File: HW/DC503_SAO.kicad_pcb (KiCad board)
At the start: 2 copper layers, 63.1 x 45.1 mm, 34 parts, among them J1 GS2, J2 GS2, U1 ATTINY85-20SU, X1 Badgelife_shitty_connector

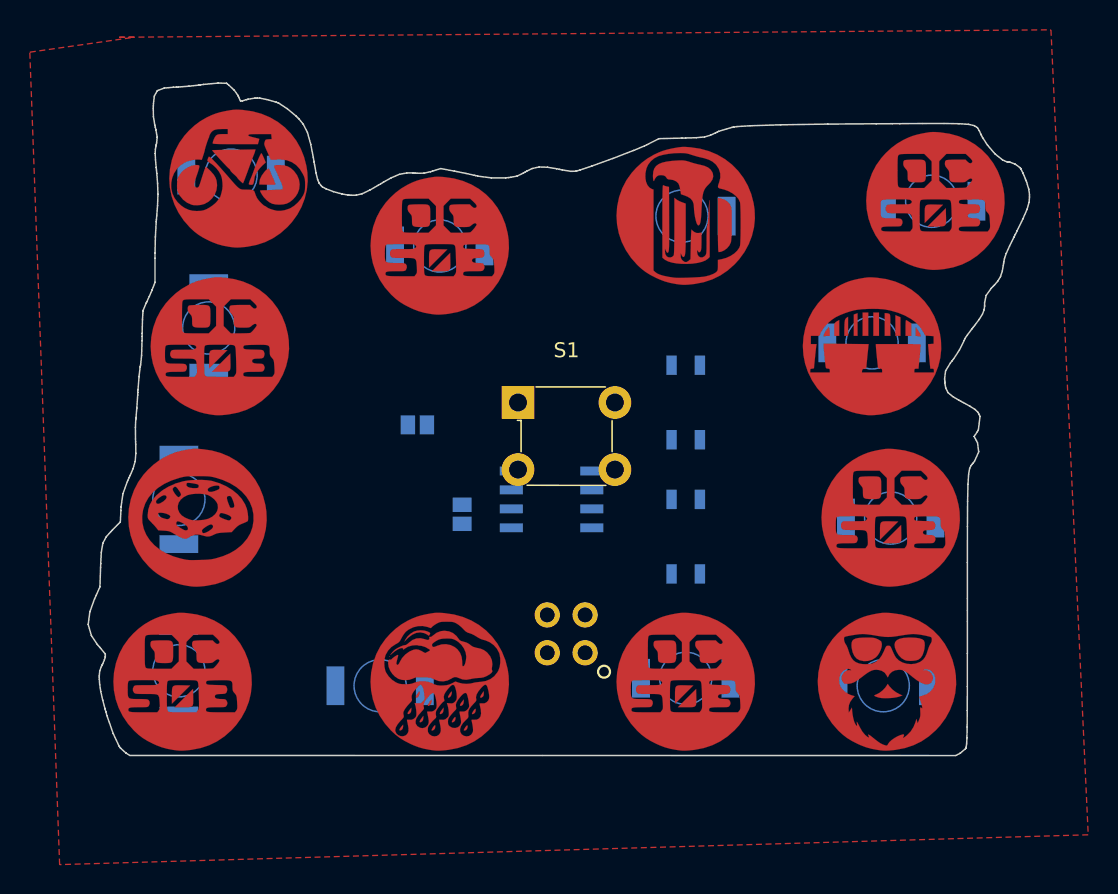
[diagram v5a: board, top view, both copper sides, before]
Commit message: Removed Silk screen from SAO CX placed LEDs move LED ref silk
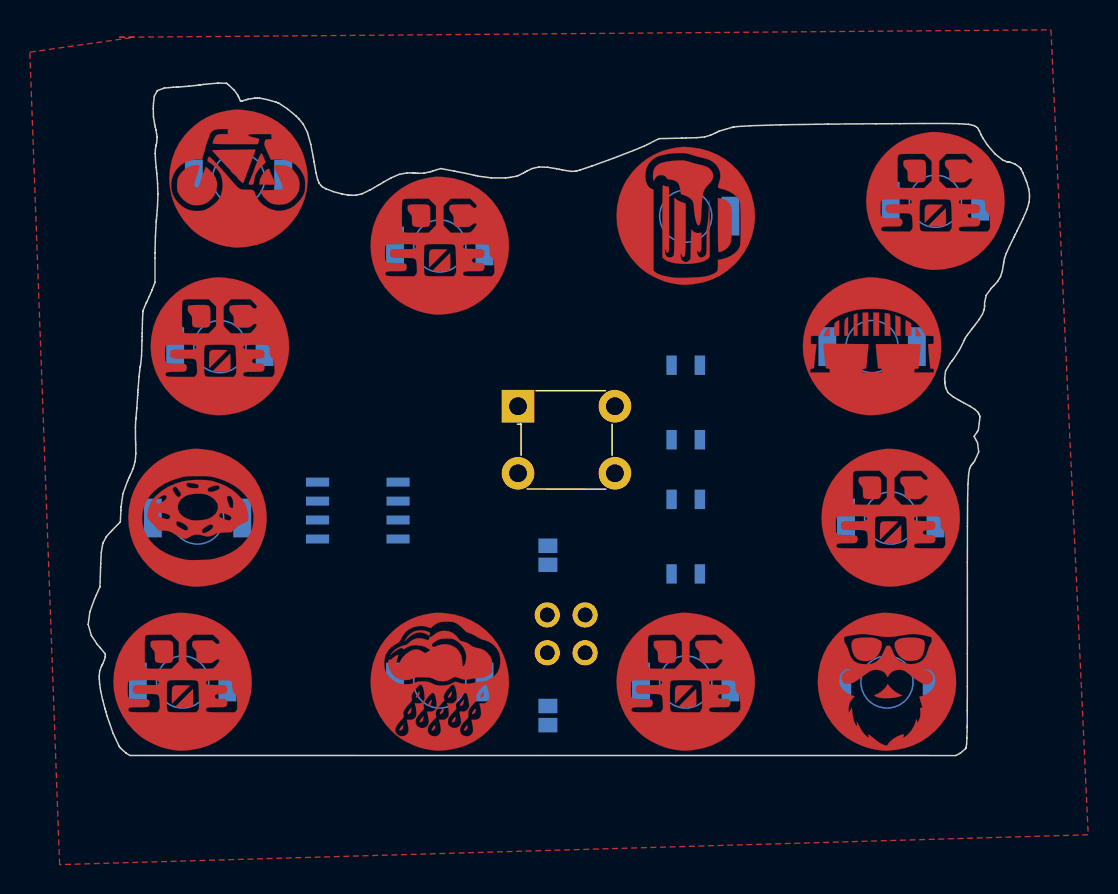
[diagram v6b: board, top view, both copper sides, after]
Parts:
- D1: footprint DC503_SAO:OSRAM_LED -> OSRAM_LED
- moved J2 14.7 mm to (173.8, 106.5)
- moved U1 13.0 mm to (161.0, 92.8)
- moved J1 12.4 mm to (173.8, 95.8), turned to 180 degrees
- moved D9 4.01 mm to (166.5, 104.2), turned to 180 degrees
- moved D11 1.77 mm to (150.2, 93.2), turned to 180 degrees
- moved D12 1.46 mm to (151.8, 81.8), turned to 180 degrees
- moved D10 0.79 mm to (149.2, 104.2), turned to 180 degrees
- moved D1 0.56 mm to (153.0, 70.5)
- moved D7 0.35 mm to (196.5, 104.2)
- moved D3 0.25 mm to (183.0, 73.0)
- moved D4 0.25 mm to (199.8, 72.0)
- moved D5 0.25 mm to (195.5, 81.8)
- moved D8 0.25 mm to (183.0, 104.2), turned to 180 degrees
- moved S1 0.25 mm to (171.8, 85.8)

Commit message: Fixed D12 wiring, Added Labels to LED nets
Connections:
- net Net-(D1-Pad2) renamed /ROW_1
- net Net-(D10-Pad2) renamed /ROW_4
- net Net-(D4-Pad2) renamed /ROW_2
- net Net-(D7-Pad2) renamed /ROW_3
- D11 pad 1: /ROW3 -> /ROW2
- D12 pad 1: /ROW4 -> /ROW3

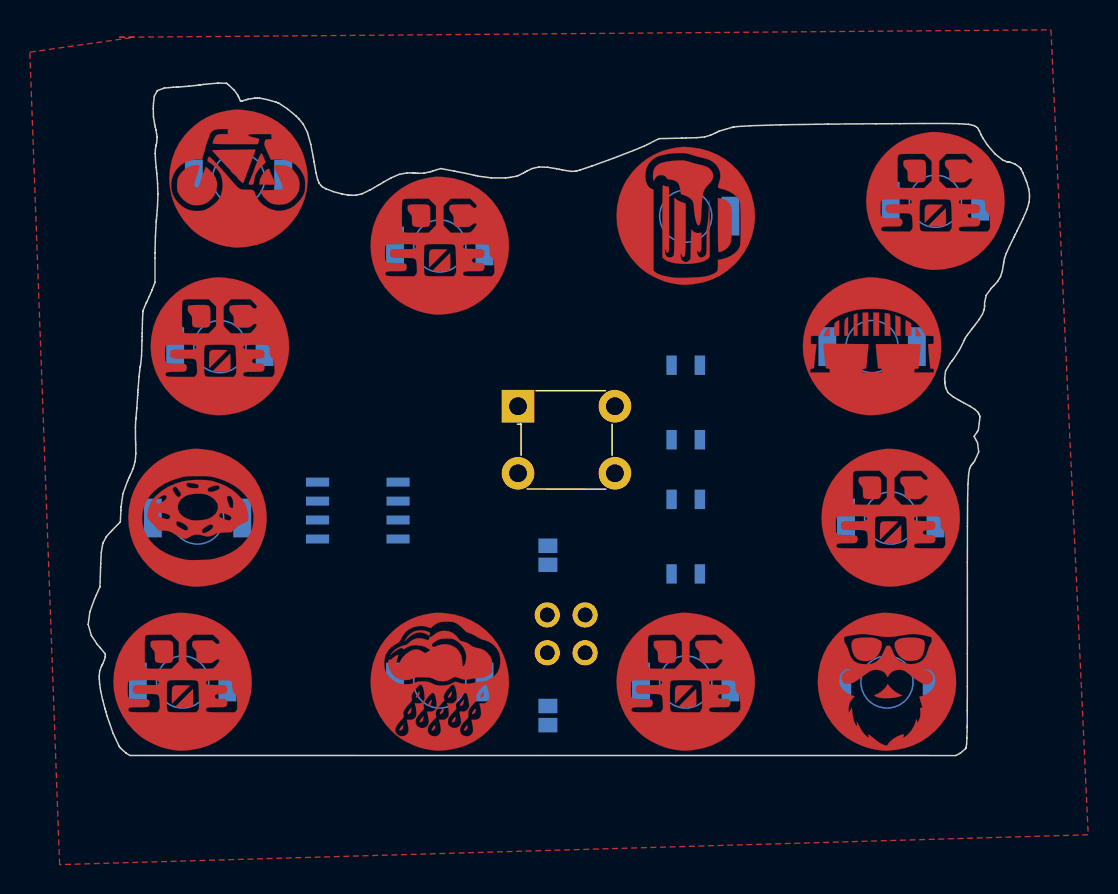
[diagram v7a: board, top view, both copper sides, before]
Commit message: Fixed the LED footprint silk for the correct polarity. Layout updated with correct footprints
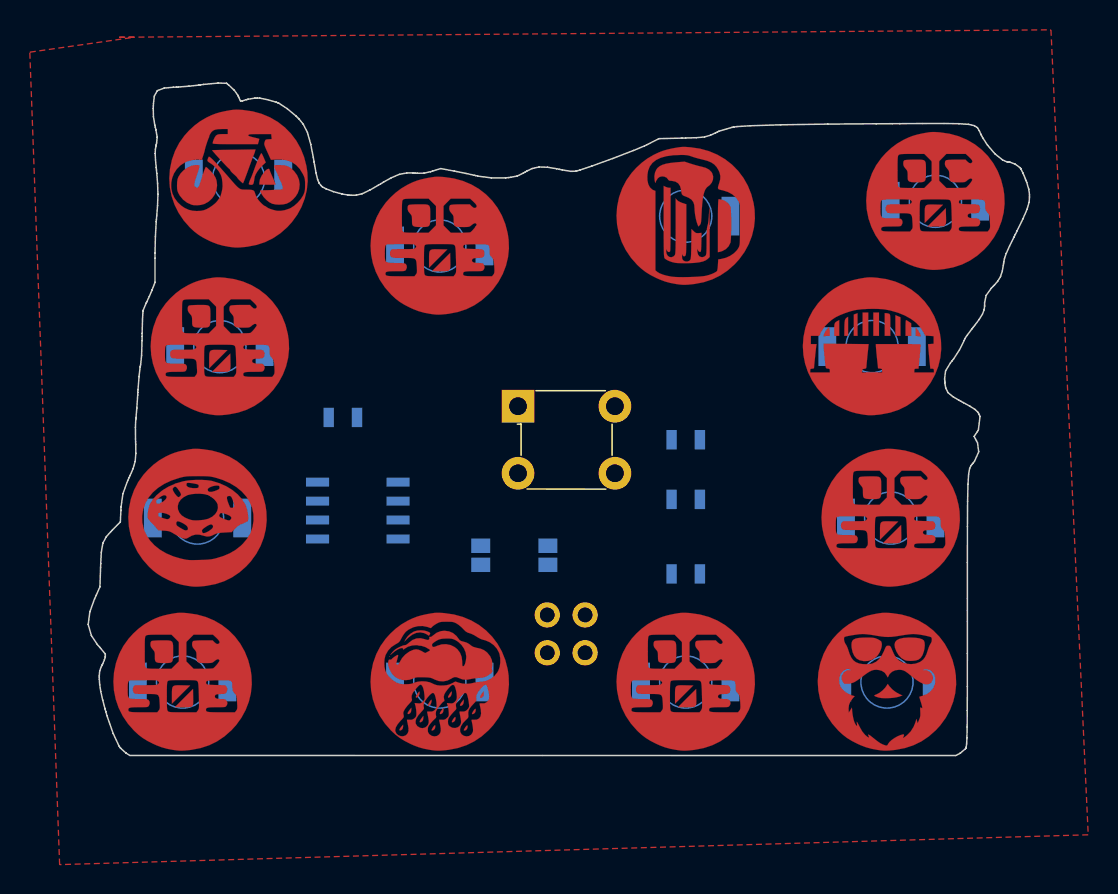
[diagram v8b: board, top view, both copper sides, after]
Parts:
- D1: footprint OSRAM_LED -> DC503_SAO:OSRAM_LED
- moved R2 23.3 mm to (160.0, 86.5)
- moved J2 11.7 mm to (169.2, 95.8), turned to 180 degrees
